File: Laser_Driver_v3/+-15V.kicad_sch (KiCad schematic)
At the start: 19 parts, among them U12 TPS7A39, U15 LT3042EDD +15V, U16 LT3094 -15V

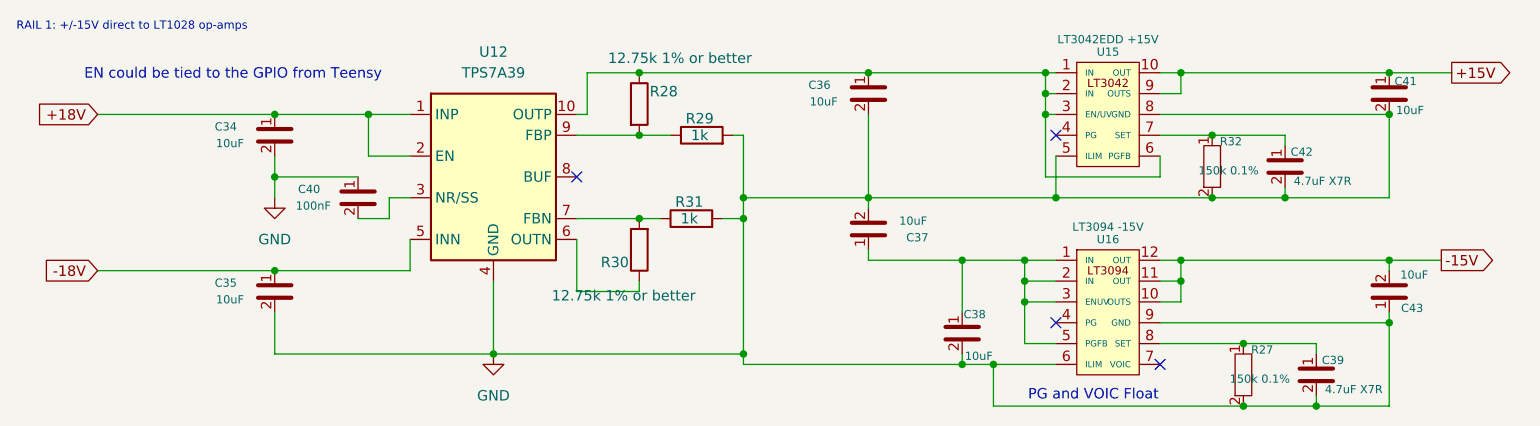
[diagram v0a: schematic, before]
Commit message: Renumbered schematics, corrections, power verified
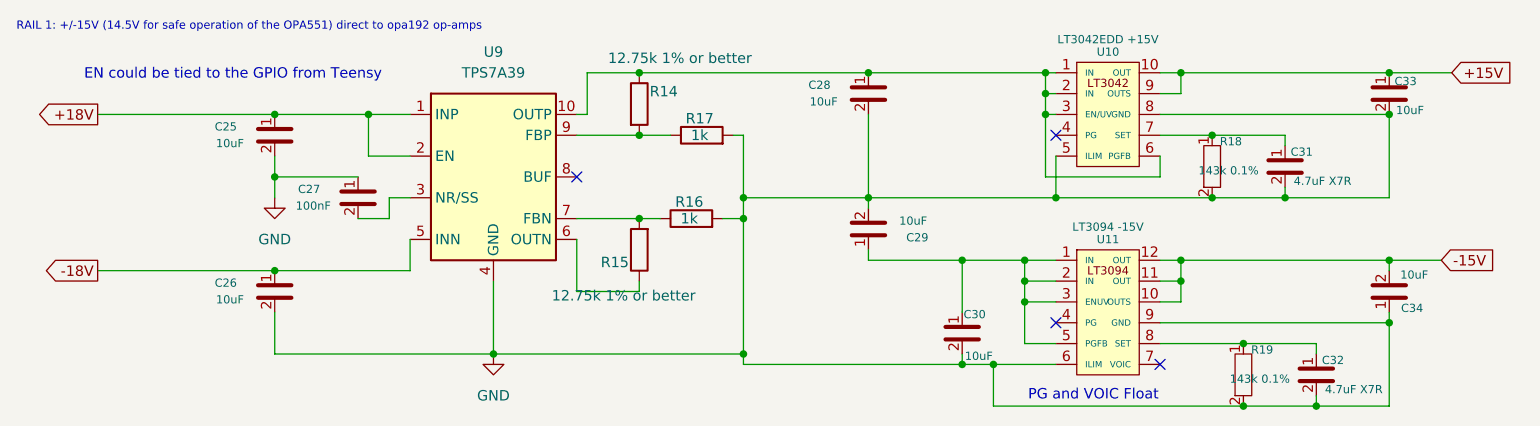
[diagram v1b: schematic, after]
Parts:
- R18: renamed from R32; value 150k 0.1% -> 143k 0.1%
- R19: renamed from R27; value 150k 0.1% -> 143k 0.1%
- renumbered C34 to C25, C35 to C26, C40 to C27, C36 to C28, C37 to C29, C38 to C30, C42 to C31, C39 to C32, C41 to C33, C43 to C34, R28 to R14, R30 to R15, R31 to R16, R29 to R17, U15 to U10, U16 to U11, U12 to U9
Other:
- note added: "RAIL 1: +/-15V (14.5V for safe operation of the OPA551) direct to opa192 op-amps"
- note removed: "RAIL 1: +/-15V direct to LT1028 op-amps"
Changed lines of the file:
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@@
 	(generator_version "10.0")
 	(paper "A4")
-	(text "RAIL 1: +/-15V direct to LT1028 op-amps"
+	(text "RAIL 1: +/-15V (14.5V for safe operation of the OPA551) direct to opa192 op-amps"
 		(exclude_from_sim no)
 		(at 54.864 49.022 0)
@@
 	)
 	(global_label "+15V"
-		(shape output)
+		(shape input)
 		(at 229.87 54.61 0)
 		(fields_autoplaced yes)
@@
 	)
 	(global_label "+18V"
-		(shape input)
+		(shape output)
 		(at 64.77 59.69 180)
 		(fields_autoplaced yes)
@@
 	)
 	(global_label "-18V"
-		(shape input)
+		(shape output)
 		(at 64.77 78.74 180)
 		(fields_autoplaced yes)
@@
 	)
 	(global_label "-15V"
-		(shape output)
+		(shape input)
 		(at 228.6 77.47 0)
 		(fields_autoplaced yes)
@@
 		(in_pos_files yes)
 		(dnp no)
-		(property "Reference" "C37"
+		(property "Reference" "C29"
 			(at 164.714 74.704 0)
 			(show_name no)
@@
 			(project "laser_driver_v3"
 				(path "/b2c3d4e5-f6a7-8901-bcde-f12345678901/9e8b43e2-3f50-408f-92ae-40d797615721"
-					(reference "C37")
+					(reference "C29")
 					(unit 1)
 				)
@@
 		(in_pos_files yes)
 		(dnp no)
-		(property "Reference" "R28"
+		(property "Reference" "R14"
 			(at 132.08 56.896 0)
 			(show_name no)
@@
 			(project "laser_driver_v3"
 				(path "/b2c3d4e5-f6a7-8901-bcde-f12345678901/9e8b43e2-3f50-408f-92ae-40d797615721"
-					(reference "R28")
+					(reference "R14")
 					(unit 1)
 				)
@@
 		(in_pos_files yes)
 		(dnp no)
-		(property "Reference" "U16"
+		(property "Reference" "U11"
 			(at 187.96 74.93 0)
 			(show_name no)
@@
 			(project "laser_driver_v3"
 				(path "/b2c3d4e5-f6a7-8901-bcde-f12345678901/9e8b43e2-3f50-408f-92ae-40d797615721"
-					(reference "U16")
+					(reference "U11")
 					(unit 1)
 				)
@@
 		(dnp no)
 		(fields_autoplaced yes)
-		(property "Reference" "#PWR08"
+		(property "Reference" "#PWR09"
 			(at 113.03 95.25 0)
 			(hide yes)
@@
 			(project "laser_driver_v3"
 				(path "/b2c3d4e5-f6a7-8901-bcde-f12345678901/9e8b43e2-3f50-408f-92ae-40d797615721"
-					(reference "#PWR08")
+					(reference "#PWR09")
 					(unit 1)
 				)
@@
 		(in_pos_files yes)
 		(dnp no)
-		(property "Reference" "C34"
+		(property "Reference" "C25"
 			(at 80.396 61.186 0)
 			(show_name no)
@@
 			(project "laser_driver_v3"
 				(path "/b2c3d4e5-f6a7-8901-bcde-f12345678901/9e8b43e2-3f50-408f-92ae-40d797615721"
-					(reference "C34")
+					(reference "C25")
 					(unit 1)
 				)
@@
 		(dnp no)
 		(fields_autoplaced yes)
-		(property "Reference" "U12"
+		(property "Reference" "U9"
 			(at 113.03 52.07 0)
 			(show_name no)
@@
 			(project "laser_driver_v3"
 				(path "/b2c3d4e5-f6a7-8901-bcde-f12345678901/9e8b43e2-3f50-408f-92ae-40d797615721"
-					(reference "U12")
+					(reference "U9")
 					(unit 1)
 				)
@@
 		(in_pos_files yes)
 		(dnp no)
-		(property "Reference" "R32"
+		(property "Reference" "R18"
 			(at 202.946 62.992 0)
 			(show_name no)
@@
 			)
 		)
-		(property "Value" "150k 0.1%"
+		(property "Value" "143k 0.1%"
 			(at 202.66 66.54 0)
 			(show_name no)
@@
 			(project "laser_driver_v3"
 				(path "/b2c3d4e5-f6a7-8901-bcde-f12345678901/9e8b43e2-3f50-408f-92ae-40d797615721"
-					(reference "R32")
+					(reference "R18")
 					(unit 1)
 				)
@@
 		(in_pos_files yes)
 		(dnp no)
-		(property "Reference" "R30"
+		(property "Reference" "R15"
 			(at 129.54 77.724 0)
 			(show_name no)
@@
 			(project "laser_driver_v3"
 				(path "/b2c3d4e5-f6a7-8901-bcde-f12345678901/9e8b43e2-3f50-408f-92ae-40d797615721"
-					(reference "R30")
+					(reference "R15")
 					(unit 1)
 				)
@@
 		(in_pos_files yes)
 		(dnp no)
-		(property "Reference" "C43"
+		(property "Reference" "C34"
 			(at 225.044 83.312 0)
 			(show_name no)
@@
 			(project "laser_driver_v3"
 				(path "/b2c3d4e5-f6a7-8901-bcde-f12345678901/9e8b43e2-3f50-408f-92ae-40d797615721"
-					(reference "C43")
+					(reference "C34")
 					(unit 1)
 				)
@@
 		(in_pos_files yes)
 		(dnp no)
-		(property "Reference" "R27"
+		(property "Reference" "R19"
 			(at 206.756 88.392 0)
 			(show_name no)
@@
 			)
 		)
-		(property "Value" "150k 0.1%"
+		(property "Value" "143k 0.1%"
 			(at 206.47 91.94 0)
 			(show_name no)
@@
 			(project "laser_driver_v3"
 				(path "/b2c3d4e5-f6a7-8901-bcde-f12345678901/9e8b43e2-3f50-408f-92ae-40d797615721"
-					(reference "R27")
+					(reference "R19")
 					(unit 1)
 				)
@@
 		(in_pos_files yes)
 		(dnp no)
-		(property "Reference" "C39"
+		(property "Reference" "C32"
 			(at 215.392 89.662 0)
 			(show_name no)
@@
 			(project "laser_driver_v3"
 				(path "/b2c3d4e5-f6a7-8901-bcde-f12345678901/9e8b43e2-3f50-408f-92ae-40d797615721"
-					(reference "C39")
+					(reference "C32")
 					(unit 1)
 				)
@@
 		(in_pos_files yes)
 		(dnp no)
-		(property "Reference" "C35"
+		(property "Reference" "C26"
 			(at 80.396 80.236 0)
 			(show_name no)
@@
 			(project "laser_driver_v3"
 				(path "/b2c3d4e5-f6a7-8901-bcde-f12345678901/9e8b43e2-3f50-408f-92ae-40d797615721"
-					(reference "C35")
+					(reference "C26")
 					(unit 1)
 				)
@@
 		(in_pos_files yes)
 		(dnp no)
-		(property "Reference" "U15"
+		(property "Reference" "U10"
 			(at 187.96 52.07 0)
 			(show_name no)
@@
 			(project "laser_driver_v3"
 				(path "/b2c3d4e5-f6a7-8901-bcde-f12345678901/9e8b43e2-3f50-408f-92ae-40d797615721"
-					(reference "U15")
+					(reference "U10")
 					(unit 1)
 				)
@@
 		(in_pos_files yes)
 		(dnp no)
-		(property "Reference" "C36"
+		(property "Reference" "C28"
 			(at 152.786 56.106 0)
 			(show_name no)
@@
 			(project "laser_driver_v3"
 				(path "/b2c3d4e5-f6a7-8901-bcde-f12345678901/9e8b43e2-3f50-408f-92ae-40d797615721"
-					(reference "C36")
+					(reference "C28")
 					(unit 1)
 				)
@@
 		(in_pos_files yes)
 		(dnp no)
-		(property "Reference" "C41"
+		(property "Reference" "C33"
 			(at 224.25 55.65 0)
 			(show_name no)
@@
 			(project "laser_driver_v3"
 				(path "/b2c3d4e5-f6a7-8901-bcde-f12345678901/9e8b43e2-3f50-408f-92ae-40d797615721"
-					(reference "C41")
+					(reference "C33")
 					(unit 1)
 				)
@@
 		(in_pos_files yes)
 		(dnp no)
-		(property "Reference" "C38"
+		(property "Reference" "C30"
 			(at 171.704 84.074 0)
 			(show_name no)
@@
 			(project "laser_driver_v3"
 				(path "/b2c3d4e5-f6a7-8901-bcde-f12345678901/9e8b43e2-3f50-408f-92ae-40d797615721"
-					(reference "C38")
+					(reference "C30")
 					(unit 1)
 				)
@@
 		(dnp no)
 		(fields_autoplaced yes)
-		(property "Reference" "#PWR010"
+		(property "Reference" "#PWR08"
 			(at 86.36 76.2 0)
 			(hide yes)
@@
 			(project "laser_driver_v3"
 				(path "/b2c3d4e5-f6a7-8901-bcde-f12345678901/9e8b43e2-3f50-408f-92ae-40d797615721"
-					(reference "#PWR010")
+					(reference "#PWR08")
 					(unit 1)
 				)
@@
 		(in_pos_files yes)
 		(dnp no)
-		(property "Reference" "C42"
+		(property "Reference" "C31"
 			(at 211.582 64.262 0)
 			(show_name no)
@@
 			(project "laser_driver_v3"
 				(path "/b2c3d4e5-f6a7-8901-bcde-f12345678901/9e8b43e2-3f50-408f-92ae-40d797615721"
-					(reference "C42")
+					(reference "C31")
 					(unit 1)
 				)
@@
 		(in_pos_files yes)
 		(dnp no)
-		(property "Reference" "C40"
+		(property "Reference" "C27"
 			(at 90.556 68.806 0)
 			(show_name no)
@@
 			(project "laser_driver_v3"
 				(path "/b2c3d4e5-f6a7-8901-bcde-f12345678901/9e8b43e2-3f50-408f-92ae-40d797615721"
-					(reference "C40")
+					(reference "C27")
 					(unit 1)
 				)
@@
 		(in_pos_files yes)
 		(dnp no)
-		(property "Reference" "R29"
+		(property "Reference" "R17"
 			(at 138.176 60.198 90)
 			(show_name no)
@@
 			(project "laser_driver_v3"
 				(path "/b2c3d4e5-f6a7-8901-bcde-f12345678901/9e8b43e2-3f50-408f-92ae-40d797615721"
-					(reference "R29")
+					(reference "R17")
 					(unit 1)
 				)
@@
 		(in_pos_files yes)
 		(dnp no)
-		(property "Reference" "R31"
+		(property "Reference" "R16"
 			(at 136.906 70.358 90)
 			(show_name no)
@@
 			(project "laser_driver_v3"
 				(path "/b2c3d4e5-f6a7-8901-bcde-f12345678901/9e8b43e2-3f50-408f-92ae-40d797615721"
-					(reference "R31")
+					(reference "R16")
 					(unit 1)
 				)
